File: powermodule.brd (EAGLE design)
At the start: 19.1 x 20.3 mm, 28 parts, among them T1 MMUN2133LT1G, U1 TPS61090RSAR, U2 MCP73871

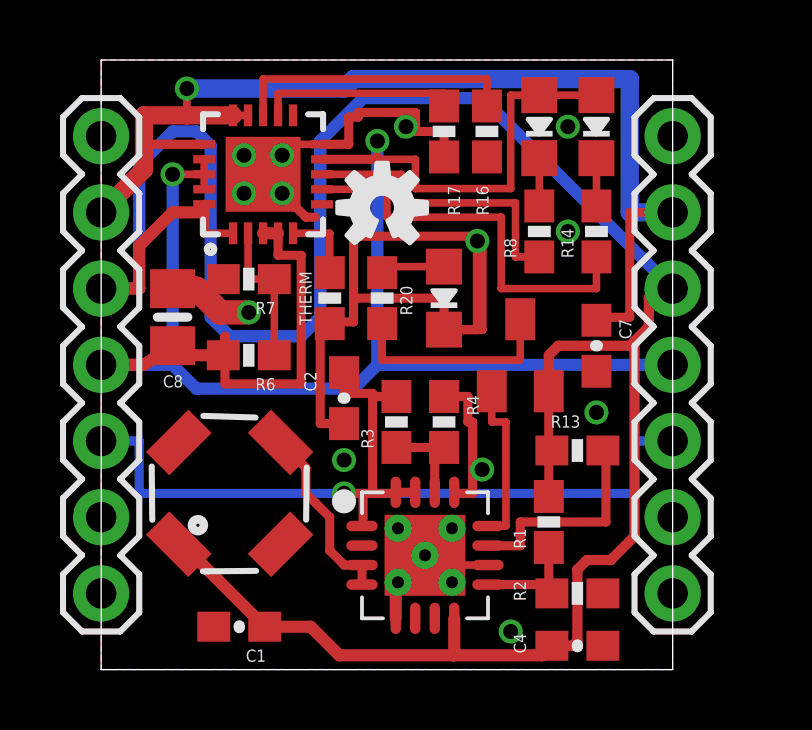
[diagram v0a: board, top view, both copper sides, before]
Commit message: Slight layout change to remove some 90 degree bends
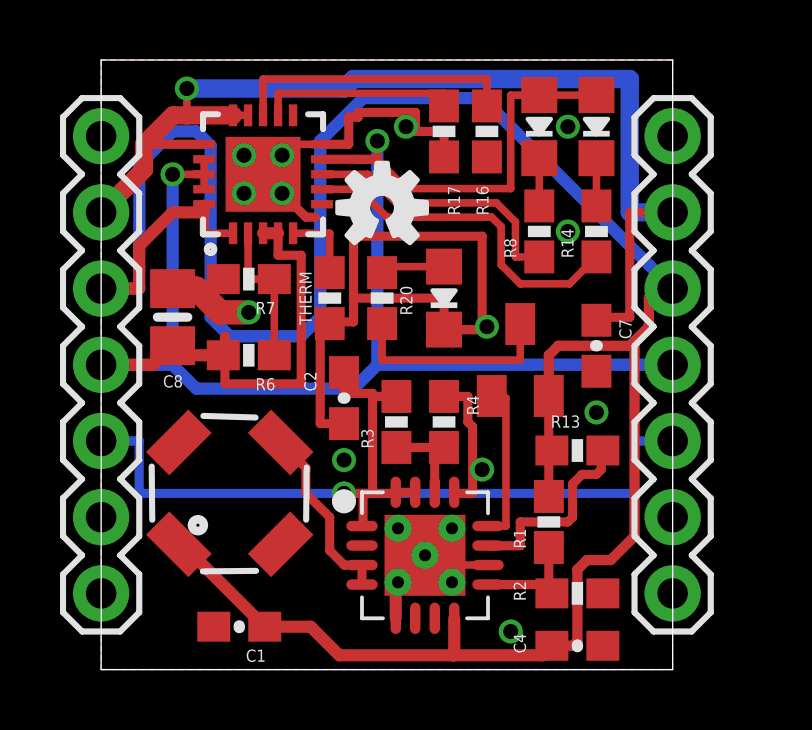
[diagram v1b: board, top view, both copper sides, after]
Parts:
- moved T1 0.16 mm to (14.0, 10.3)
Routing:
- net GND: track 52.6 -> 49.8 mm
- net C_DONE: track 13.5 -> 11.6 mm
- net VBUS: track 66.9 -> 65.2 mm
- net C_LBO: track 10.00 -> 9.07 mm
- net VLIPO: track 38.6 -> 38.1 mm
- net ENABLE: track 7.22 -> 6.71 mm

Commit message: Slight improvement to ground coverage
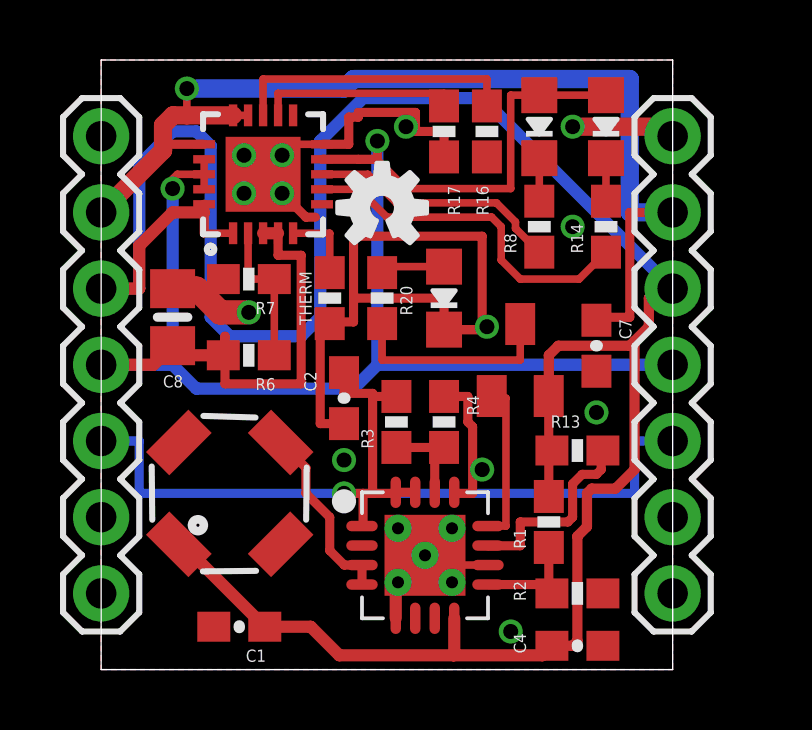
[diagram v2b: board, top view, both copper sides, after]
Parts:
- moved R14 0.35 mm to (16.8, 14.8)
- moved DONE 0.32 mm to (16.8, 18.1)
- moved R8 0.16 mm to (14.6, 14.8)
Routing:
- net GND: track 49.8 -> 53.3 mm
- net C_LBO: track 9.07 -> 8.44 mm
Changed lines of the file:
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@@
 </element>
 <element name="CHRG/LBO" library="microbuilder" package="CHIPLED_0805_NOOUTLINE" value="ORANGE" x="14.605" y="18.0975" smashed="yes" rot="R180"/>
-<element name="DONE" library="microbuilder" package="CHIPLED_0805_NOOUTLINE" value="GREEN" x="16.51" y="18.0975" smashed="yes" rot="R180"/>
+<element name="DONE" library="microbuilder" package="CHIPLED_0805_NOOUTLINE" value="GREEN" x="16.8275" y="18.0975" smashed="yes" rot="R180"/>
 <element name="L1" library="SparkFun-Passives" package="SRU5028" value="6.8uH" x="4.28625" y="5.87375" smashed="yes" rot="R225"/>
 <element name="LED1" library="microbuilder" package="CHIPLED_0805_NOOUTLINE" value="RED" x="11.43" y="12.3825" smashed="yes" rot="R180"/>
@@
 <attribute name="NAME" x="14.986" y="8.0645" size="0.4064" layer="25" font="vector"/>
 </element>
-<element name="R14" library="SparkFun-Resistors" package="0603-RES" value="1K" x="16.51" y="14.605" smashed="yes" rot="R90">
-<attribute name="NAME" x="15.748" y="13.716" size="0.4064" layer="25" font="vector" rot="R90"/>
+<element name="R14" library="SparkFun-Resistors" package="0603-RES" value="1K" x="16.8275" y="14.76375" smashed="yes" rot="R90">
+<attribute name="NAME" x="16.0655" y="13.87475" size="0.4064" layer="25" font="vector" rot="R90"/>
 </element>
 <element name="R16" library="SparkFun-Resistors" package="0603-RES" value="1.0K" x="12.85875" y="17.93875" smashed="yes" rot="R90">
@@
 <attribute name="NAME" x="5.81025" y="12.2555" size="0.4064" layer="25" font="vector" rot="R180"/>
 </element>
-<element name="R8" library="SparkFun-Resistors" package="0603-RES" value="1K" x="14.605" y="14.605" smashed="yes" rot="R90">
-<attribute name="NAME" x="13.843" y="13.716" size="0.4064" layer="25" font="vector" rot="R90"/>
+<element name="R8" library="SparkFun-Resistors" package="0603-RES" value="1K" x="14.605" y="14.76375" smashed="yes" rot="R90">
+<attribute name="NAME" x="13.843" y="13.87475" size="0.4064" layer="25" font="vector" rot="R90"/>
 </element>
 <element name="T1" library="transistor" package="SC59-BEC" value="MMUN2133LT1G" x="13.97" y="10.31875" smashed="yes"/>
@@
 <wire x1="10.4775" y1="17.93875" x2="11.43" y2="17.93875" width="0.3048" layer="1"/>
 <wire x1="11.43" y1="17.93875" x2="11.43" y2="17.08875" width="0.3048" layer="1"/>
-<via x="15.5575" y="18.0975" extent="1-16" drill="0.5" diameter="0.4064"/>
+<via x="15.71625" y="18.0975" extent="1-16" drill="0.5" diameter="0.4064"/>
 <via x="12.85875" y="11.43" extent="1-16" drill="0.5" diameter="0.4064"/>
 <via x="10.16" y="18.0975" extent="1-16" drill="0.5" diameter="0.4064"/>
-<via x="15.5575" y="14.605" extent="1-16" drill="0.5" diameter="0.4064"/>
+<via x="15.71625" y="14.76375" extent="1-16" drill="0.5" diameter="0.4064"/>
 <wire x1="4.7625" y1="15.875" x2="6.0325" y2="15.875" width="0.3048" layer="1"/>
 <wire x1="6.0325" y1="15.875" x2="6.82625" y2="15.08125" width="0.3048" layer="1"/>
@@
 <wire x1="7.3025" y1="11.43" x2="7.3025" y2="8.19875" width="0.3048" layer="1"/>
 <wire x1="7.3025" y1="8.19875" x2="8.09625" y2="8.19875" width="0.3048" layer="1"/>
+<wire x1="19.05" y1="17.78" x2="18.7325" y2="18.0975" width="0.6096" layer="1"/>
+<wire x1="18.7325" y1="18.0975" x2="15.71625" y2="18.0975" width="0.6096" layer="1"/>
 </signal>
 <signal name="N$1">
@@
 <wire x1="15.025" y1="0.79375" x2="15.71625" y2="0.79375" width="0.3429" layer="1"/>
 <wire x1="15.71625" y1="0.79375" x2="15.875" y2="0.9525" width="0.3429" layer="1"/>
-<wire x1="15.875" y1="0.9525" x2="15.875" y2="3.33375" width="0.3429" layer="1"/>
-<wire x1="15.875" y1="3.33375" x2="16.1925" y2="3.65125" width="0.3429" layer="1"/>
-<wire x1="16.1925" y1="3.65125" x2="16.98625" y2="3.65125" width="0.3429" layer="1"/>
-<wire x1="16.98625" y1="3.65125" x2="17.78" y2="4.445" width="0.3429" layer="1"/>
-<wire x1="17.78" y1="4.445" x2="17.78" y2="10.95375" width="0.3429" layer="1"/>
+<wire x1="15.875" y1="0.9525" x2="15.875" y2="4.445" width="0.3429" layer="1"/>
+<wire x1="15.875" y1="4.445" x2="16.1925" y2="4.7625" width="0.3429" layer="1"/>
+<wire x1="16.1925" y1="4.7625" x2="16.1925" y2="5.87375" width="0.3429" layer="1"/>
+<wire x1="16.1925" y1="5.87375" x2="16.35125" y2="6.0325" width="0.3429" layer="1"/>
+<wire x1="16.35125" y1="6.0325" x2="17.145" y2="6.0325" width="0.3429" layer="1"/>
+<wire x1="17.145" y1="6.0325" x2="17.78" y2="6.6675" width="0.3429" layer="1"/>
+<wire x1="17.78" y1="6.6675" x2="17.78" y2="10.95375" width="0.3429" layer="1"/>
 <wire x1="17.78" y1="10.95375" x2="18.25625" y2="11.43" width="0.3429" layer="1"/>
 </signal>
@@
 <wire x1="9.525" y1="15.08125" x2="13.0175" y2="15.08125" width="0.254" layer="1"/>
 <wire x1="13.0175" y1="15.08125" x2="13.335" y2="14.76375" width="0.254" layer="1"/>
-<wire x1="13.335" y1="14.76375" x2="13.335" y2="13.49375" width="0.254" layer="1"/>
-<wire x1="13.335" y1="13.49375" x2="13.97" y2="12.85875" width="0.254" layer="1"/>
-<wire x1="13.97" y1="12.85875" x2="15.61375" y2="12.85875" width="0.254" layer="1"/>
-<wire x1="15.61375" y1="12.85875" x2="16.51" y2="13.755" width="0.254" layer="1"/>
+<wire x1="13.335" y1="14.76375" x2="13.335" y2="13.6525" width="0.254" layer="1"/>
+<wire x1="13.335" y1="13.6525" x2="13.97" y2="13.0175" width="0.254" layer="1"/>
+<wire x1="13.97" y1="13.0175" x2="15.93125" y2="13.0175" width="0.254" layer="1"/>
+<wire x1="15.93125" y1="13.0175" x2="16.8275" y2="13.91375" width="0.254" layer="1"/>
 </signal>
 <signal name="C_LBO">
 <contactref element="R8" pad="1"/>
 <contactref element="U2" pad="P$8"/>
-<wire x1="14.605" y1="13.755" x2="13.81125" y2="13.755" width="0.254" layer="1"/>
+<wire x1="14.605" y1="13.91375" x2="13.81125" y2="14.7075" width="0.254" layer="1"/>
 <wire x1="9.8425" y1="15.5575" x2="8.89" y2="16.51" width="0.254" layer="1"/>
 <wire x1="8.89" y1="16.51" x2="7.3625" y2="16.51" width="0.254" layer="1"/>
 <wire x1="9.8425" y1="15.5575" x2="13.17625" y2="15.5575" width="0.254" layer="1"/>
 <wire x1="13.17625" y1="15.5575" x2="13.81125" y2="14.9225" width="0.254" layer="1"/>
-<wire x1="13.81125" y1="14.9225" x2="13.81125" y2="13.755" width="0.254" layer="1"/>
+<wire x1="13.81125" y1="14.9225" x2="13.81125" y2="14.7075" width="0.254" layer="1"/>
 </signal>
 <signal name="N$16">
@@
 <contactref element="J3" pad="4"/>
 <contactref element="J4" pad="4"/>
-<wire x1="16.51" y1="19.1475" x2="14.605" y2="19.1475" width="0.254" layer="1"/>
+<wire x1="16.8275" y1="19.1475" x2="14.605" y2="19.1475" width="0.254" layer="1"/>
 <wire x1="13.6525" y1="16.03375" x2="13.6525" y2="19.1475" width="0.254" layer="1"/>
 <wire x1="14.605" y1="19.1475" x2="13.6525" y2="19.1475" width="0.254" layer="1"/>
@@
 <wire x1="3.4325" y1="16.01" x2="3.4325" y2="16.51" width="0.254" layer="1"/>
 <wire x1="3.4325" y1="17.01" x2="3.4325" y2="16.51" width="0.254" layer="1"/>
-<wire x1="3.4325" y1="16.51" x2="2.38125" y2="16.51" width="0.254" layer="1"/>
-<via x="2.38125" y="16.51" extent="1-16" drill="0.5" diameter="0.4064"/>
-<wire x1="2.38125" y1="16.51" x2="2.38125" y2="10.16" width="0.4064" layer="16"/>
+<wire x1="3.4325" y1="16.51" x2="2.54" y2="16.51" width="0.254" layer="1"/>
+<wire x1="2.54" y1="16.51" x2="2.38125" y2="16.35125" width="0.254" layer="1"/>
+<wire x1="2.38125" y1="16.35125" x2="2.38125" y2="16.03375" width="0.254" layer="1"/>
+<via x="2.38125" y="16.03375" extent="1-16" drill="0.5" diameter="0.4064"/>
+<wire x1="2.38125" y1="16.03375" x2="2.38125" y2="10.16" width="0.4064" layer="16"/>
 <wire x1="2.38125" y1="10.16" x2="3.175" y2="9.36625" width="0.4064" layer="16"/>
 <wire x1="19.05" y1="10.16" x2="9.2075" y2="10.16" width="0.4064" layer="16"/>
@@
 <contactref element="J3" pad="6"/>
 <contactref element="J4" pad="6"/>
-<wire x1="0" y1="15.24" x2="1.42875" y2="16.66875" width="0.6096" layer="1"/>
-<wire x1="1.42875" y1="16.66875" x2="1.42875" y2="17.51" width="0.6096" layer="1"/>
+<wire x1="0" y1="15.24" x2="2.06375" y2="17.30375" width="0.6096" layer="1"/>
+<wire x1="2.06375" y1="17.30375" x2="2.06375" y2="18.145" width="0.6096" layer="1"/>
 <wire x1="2.8575" y1="18.475" x2="4.3975" y2="18.475" width="0.6096" layer="1"/>
-<wire x1="3.4325" y1="17.51" x2="1.42875" y2="17.51" width="0.3048" layer="1"/>
+<wire x1="3.4325" y1="17.51" x2="2.175" y2="17.51" width="0.3048" layer="1"/>
+<wire x1="2.175" y1="17.51" x2="2.06375" y2="17.62125" width="0.3048" layer="1"/>
+<wire x1="2.06375" y1="17.62125" x2="2.06375" y2="18.145" width="0.3048" layer="1"/>
 <wire x1="17.62125" y1="11.745" x2="17.62125" y2="15.24" width="0.3048" layer="1"/>
 <wire x1="17.62125" y1="15.24" x2="19.05" y2="15.24" width="0.3048" layer="1"/>
@@
 <wire x1="17.62125" y1="15.24" x2="19.05" y2="15.24" width="0.6096" layer="16"/>
 <wire x1="2.8575" y1="18.475" x2="4.8975" y2="18.475" width="0.254" layer="1"/>
-<wire x1="1.42875" y1="17.51" x2="2.39375" y2="18.475" width="0.6096" layer="1"/>
+<wire x1="2.06375" y1="18.145" x2="2.39375" y2="18.475" width="0.6096" layer="1"/>
 <wire x1="2.39375" y1="18.475" x2="2.8575" y2="18.475" width="0.6096" layer="1"/>
 </signal>
@@
 <contactref element="DONE" pad="C"/>
 <contactref element="R14" pad="2"/>
-<wire x1="16.51" y1="15.455" x2="16.51" y2="17.0475" width="0.254" layer="1"/>
+<wire x1="16.8275" y1="15.61375" x2="16.8275" y2="17.0475" width="0.254" layer="1"/>
 </signal>
 <signal name="N$12">
 <contactref element="CHRG/LBO" pad="C"/>
 <contactref element="R8" pad="2"/>
-<wire x1="14.605" y1="15.455" x2="14.605" y2="17.0475" width="0.254" layer="1"/>
+<wire x1="14.605" y1="15.61375" x2="14.605" y2="17.0475" width="0.254" layer="1"/>
 </signal>
 <signal name="N$13">

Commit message: Made board slightly wider so it fits into a breadboard right.
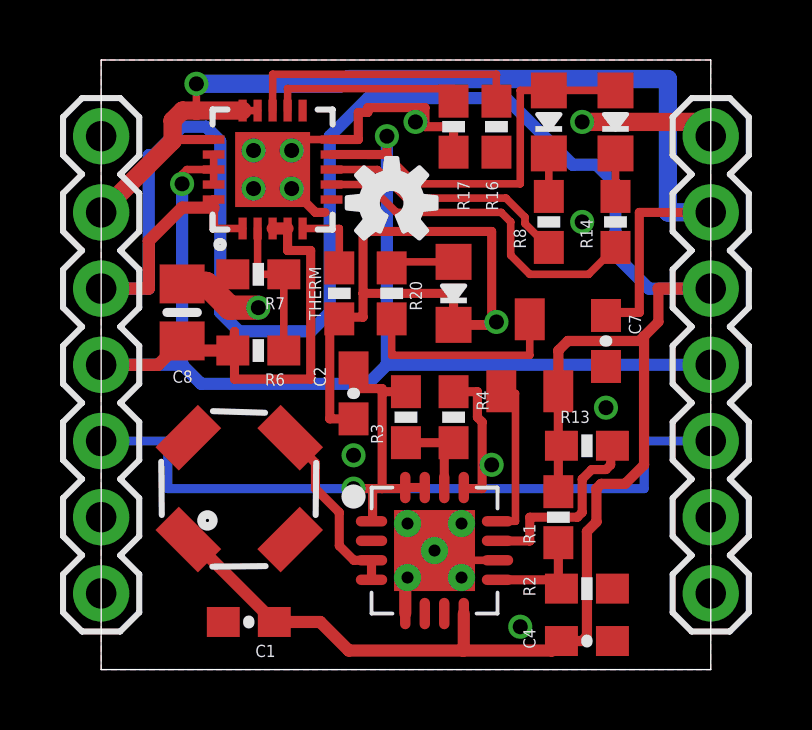
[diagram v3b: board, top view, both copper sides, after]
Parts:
- moved J4 1.27 mm to (20.3, 2.54)
- moved R17 0.35 mm to (11.7, 18.1)
- moved R1 0.35 mm to (15.2, 5.08)
- moved U1 0.35 mm to (11.1, 3.97)
- moved C2 0.35 mm to (8.41, 9.21)
- moved LED1 0.35 mm to (11.7, 12.5)
- moved R3 0.35 mm to (10.2, 8.41)
- moved R4 0.35 mm to (11.7, 8.41)
- moved R6 0.35 mm to (5.24, 10.6)
- moved C1 0.35 mm to (4.92, 1.59)
- moved C8 0.35 mm to (2.70, 11.9)
- moved L1 0.35 mm to (4.60, 6.03)
- moved R7 0.35 mm to (5.24, 13.2)
- moved THERM 0.35 mm to (7.94, 12.5)
- moved CHRG/LBO 0.35 mm to (14.9, 18.3)
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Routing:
- net VBAT: track 84.8 -> 89.0 mm
- net VLIPO: track 38.0 -> 39.9 mm
- net VBUS: track 65.4 -> 67.3 mm
- net GND: track 53.3 -> 54.3 mm
- net 5.0V: track 31.9 -> 32.8 mm
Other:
- board size 19.1 x 20.3 mm -> 20.3 x 20.3 mm
